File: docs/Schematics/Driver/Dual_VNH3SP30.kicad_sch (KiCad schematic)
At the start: 0 parts

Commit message: Add Wheel encoder
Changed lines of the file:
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@@
   (junction (at 76.2 53.34) (diameter 0) (color 0 0 0 0)
   )
-  (junction (at 132.08 62.23) (diameter 0) (color 0 0 0 0)
-  )
   (junction (at 80.01 50.8) (diameter 0) (color 0 0 0 0)
-  )
-  (junction (at 81.28 53.34) (diameter 0) (color 0 0 0 0)
   )
   (wire (pts (xy 115.57 55.88) (xy 132.08 55.88))
@@
     (stroke (width 0) (type default) (color 0 0 0 0))
   )
-  (wire (pts (xy 76.2 53.34) (xy 81.28 53.34))
-    (stroke (width 0) (type default) (color 0 0 0 0))
-  )
   (wire (pts (xy 115.57 80.01) (xy 132.08 80.01))
-    (stroke (width 0) (type default) (color 0 0 0 0))
-  )
-  (wire (pts (xy 132.08 62.23) (xy 81.28 62.23))
     (stroke (width 0) (type default) (color 0 0 0 0))
   )
@@
     (stroke (width 0) (type default) (color 0 0 0 0))
   )
-  (wire (pts (xy 81.28 53.34) (xy 83.82 53.34))
+  (wire (pts (xy 76.2 53.34) (xy 83.82 53.34))
     (stroke (width 0) (type default) (color 0 0 0 0))
   )
-  (wire (pts (xy 81.28 62.23) (xy 81.28 53.34))
-    (stroke (width 0) (type default) (color 0 0 0 0))
-  )

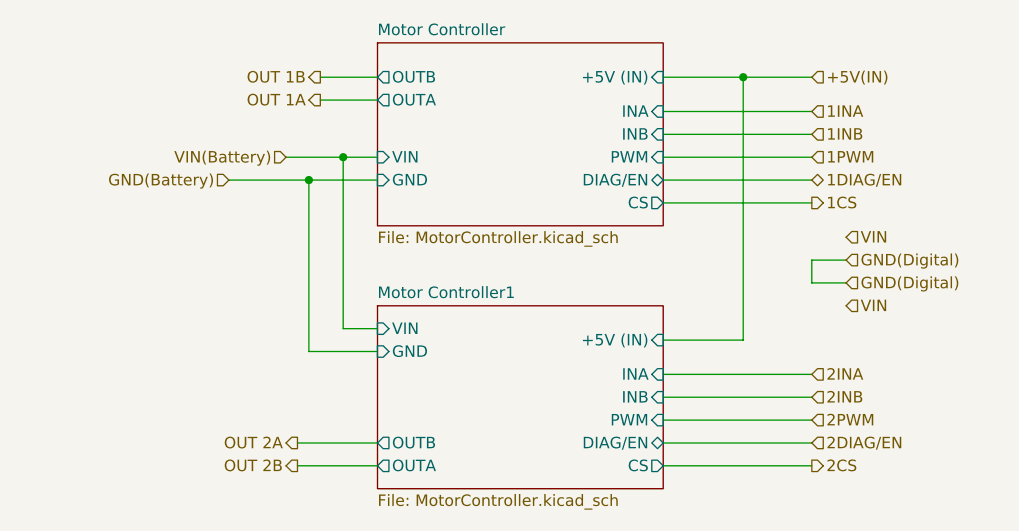
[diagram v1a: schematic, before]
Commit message: First scematic design for the card
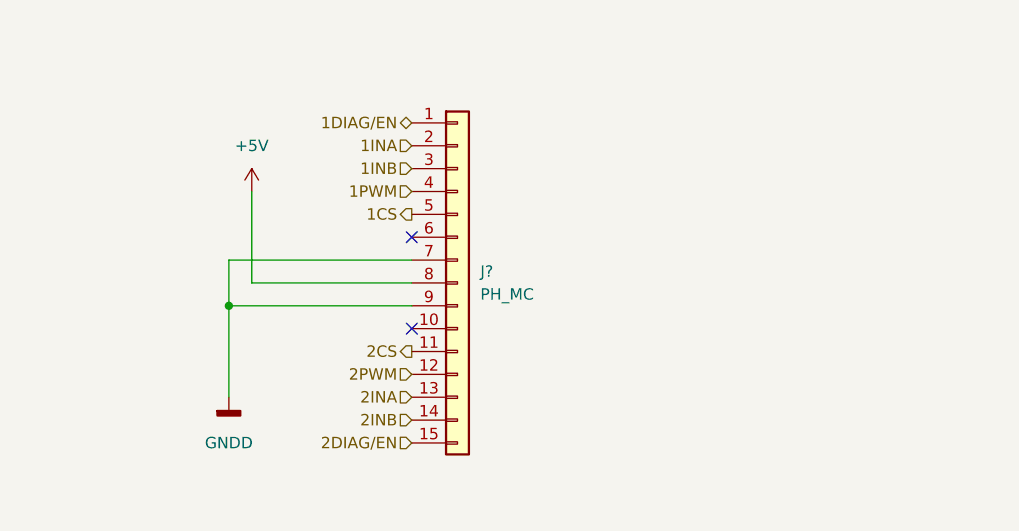
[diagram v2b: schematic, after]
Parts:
- added J?: PH_MC, symbol Connector_Generic:Conn_01x15
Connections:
- net 1CS: now also J?.5 (Pin_5)
- net 1DIAG/EN: now also J?.1 (Pin_1)
- net 1INA: now also J?.2 (Pin_2)
- net 1INB: now also J?.3 (Pin_3)
- net 1PWM: now also J?.4 (Pin_4)
- net 2CS: now also J?.11 (Pin_11)
- net 2DIAG/EN: now also J?.15 (Pin_15)
- net 2INA: now also J?.13 (Pin_13)
- net 2INB: now also J?.14 (Pin_14)
- net 2PWM: now also J?.12 (Pin_12)
- new net +5V: J?.8 (Pin_8)
- new net GNDD: J?.7 (Pin_7), J?.9 (Pin_9)
- no-connect marks 0 -> 2
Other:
- removed sheet Motor Controller
- removed sheet Motor Controller1
- company: (none) -> HiQ
- title: (none) -> Arty Z7 IO expander card

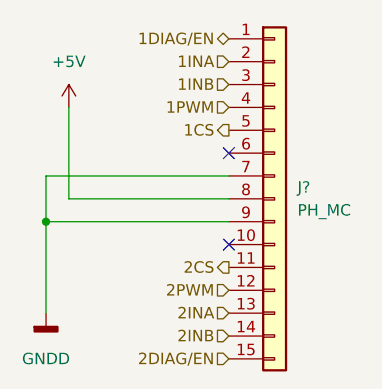
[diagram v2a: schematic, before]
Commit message: Added footprints and a symbol for the level shifters
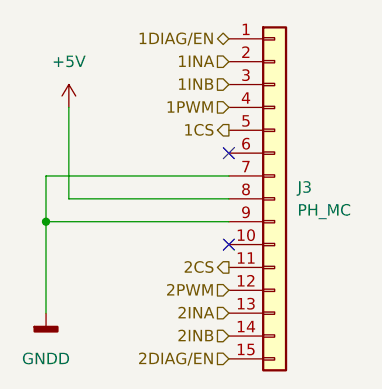
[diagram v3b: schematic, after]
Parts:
- J3: renamed from J?; footprint (none) -> Connector_PinHeader_2.54mm:PinHeader_1x15_P2.54mm_Vertical
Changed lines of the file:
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@@
   (symbol (lib_id "power:GNDD") (at 67.31 77.47 0) (unit 1)
     (in_bom yes) (on_board yes) (fields_autoplaced)
-    (property "Reference" "#PWR?" (id 0) (at 67.31 83.82 0)
+    (property "Reference" "#PWR05" (id 0) (at 67.31 83.82 0)
       (effects (font (size 1.27 1.27)) hide)
     )
@@
   (symbol (lib_id "Connector_Generic:Conn_01x15") (at 92.71 64.77 0) (unit 1)
     (in_bom yes) (on_board yes) (fields_autoplaced)
-    (property "Reference" "J?" (id 0) (at 95.25 63.4999 0)
+    (property "Reference" "J3" (id 0) (at 95.25 63.4999 0)
       (effects (font (size 1.27 1.27)) (justify left))
     )
@@
       (effects (font (size 1.27 1.27)) (justify left))
     )
-    (property "Footprint" "" (id 2) (at 92.71 64.77 0)
+    (property "Footprint" "Connector_PinHeader_2.54mm:PinHeader_1x15_P2.54mm_Vertical" (id 2) (at 92.71 64.77 0)
       (effects (font (size 1.27 1.27)) hide)
     )
@@
   (symbol (lib_id "power:+5V") (at 69.85 54.61 0) (unit 1)
     (in_bom yes) (on_board yes) (fields_autoplaced)
-    (property "Reference" "#PWR?" (id 0) (at 69.85 58.42 0)
+    (property "Reference" "#PWR06" (id 0) (at 69.85 58.42 0)
       (effects (font (size 1.27 1.27)) hide)
     )

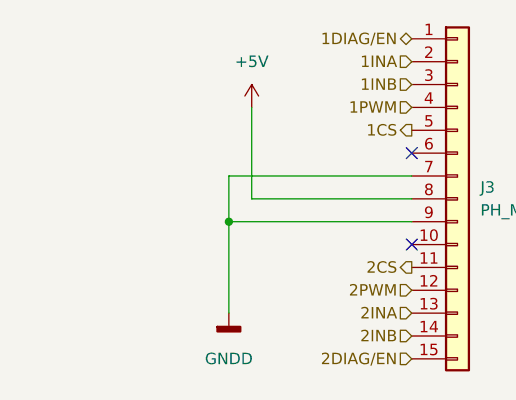
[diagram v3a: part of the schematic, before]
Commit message: Added caps and changed the connection from the motor sensors to plints
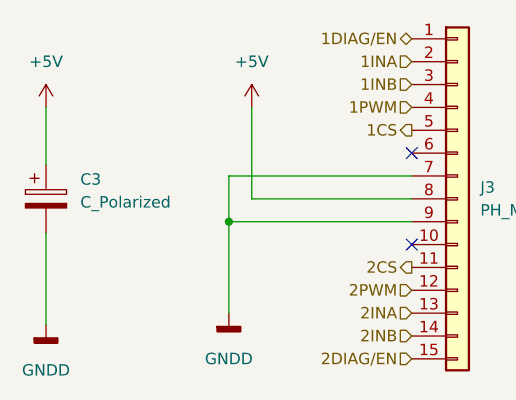
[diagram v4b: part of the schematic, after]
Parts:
- added C3: C_Polarized, Capacitor_THT:CP_Radial_D6.3mm_P2.50mm, symbol Device:C_Polarized
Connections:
- net +5V: now also C3.1
- net GNDD: now also C3.2
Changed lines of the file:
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@@
     (stroke (width 0) (type default) (color 0 0 0 0))
   )
+  (wire (pts (xy 46.99 68.58) (xy 46.99 78.74))
+    (stroke (width 0) (type default) (color 0 0 0 0))
+  )
   (wire (pts (xy 67.31 62.23) (xy 87.63 62.23))
     (stroke (width 0) (type default) (color 0 0 0 0))
@@
     (stroke (width 0) (type default) (color 0 0 0 0))
   )
+  (wire (pts (xy 46.99 54.61) (xy 46.99 60.96))
+    (stroke (width 0) (type default) (color 0 0 0 0))
+  )
   (wire (pts (xy 69.85 64.77) (xy 87.63 64.77))
     (stroke (width 0) (type default) (color 0 0 0 0))
@@
     (effects (font (size 1.27 1.27)) (justify right))
   )
+  (symbol (lib_id "Device:C_Polarized") (at 46.99 64.77 0) (unit 1)
+    (in_bom yes) (on_board yes) (fields_autoplaced)
+    (property "Reference" "C3" (id 0) (at 50.8 62.6109 0)
+      (effects (font (size 1.27 1.27)) (justify left))
+    )
+    (property "Value" "C_Polarized" (id 1) (at 50.8 65.1509 0)
+      (effects (font (size 1.27 1.27)) (justify left))
+    )
+    (property "Footprint" "Capacitor_THT:CP_Radial_D6.3mm_P2.50mm" (id 2) (at 47.9552 68.58 0)
+      (effects (font (size 1.27 1.27)) hide)
+    )
+    (property "Datasheet" "~" (id 3) (at 46.99 64.77 0)
+      (effects (font (size 1.27 1.27)) hide)
+    )
+    (pin "1")
+    (pin "2")
+  )
+  (symbol (lib_id "power:GNDD") (at 46.99 78.74 0) (unit 1)
+    (in_bom yes) (on_board yes) (fields_autoplaced)
+    (property "Reference" "#PWR044" (id 0) (at 46.99 85.09 0)
+      (effects (font (size 1.27 1.27)) hide)
+    )
+    (property "Value" "GNDD" (id 1) (at 46.99 83.82 0))
+    (property "Footprint" "" (id 2) (at 46.99 78.74 0)
+      (effects (font (size 1.27 1.27)) hide)
+    )
+    (property "Datasheet" "" (id 3) (at 46.99 78.74 0)
+      (effects (font (size 1.27 1.27)) hide)
+    )
+    (pin "1")
+  )
   (symbol (lib_id "power:GNDD") (at 67.31 77.47 0) (unit 1)
     (in_bom yes) (on_board yes) (fields_autoplaced)
@@
       (effects (font (size 1.27 1.27)) hide)
     )
+    (pin "1")
+  )
+  (symbol (lib_id "power:+5V") (at 46.99 54.61 0) (unit 1)
+    (in_bom yes) (on_board yes) (fields_autoplaced)
+    (property "Reference" "#PWR043" (id 0) (at 46.99 58.42 0)
+      (effects (font (size 1.27 1.27)) hide)
+    )
+    (property "Value" "+5V" (id 1) (at 46.99 49.53 0))
+    (property "Footprint" "" (id 2) (at 46.99 54.61 0)
+      (effects (font (size 1.27 1.27)) hide)
+    )
+    (property "Datasheet" "" (id 3) (at 46.99 54.61 0)
+      (effects (font (size 1.27 1.27)) hide)
+    )

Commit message: Started routing the pcb.
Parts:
- C3: footprint Capacitor_THT:CP_Radial_D6.3mm_P2.50mm -> Capacitor_SMD:C_0805_2012Metric_Pad1.18x1.45mm_HandSolder
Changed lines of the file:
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@@
       (effects (font (size 1.27 1.27)) (justify left))
     )
-    (property "Footprint" "Capacitor_THT:CP_Radial_D6.3mm_P2.50mm" (id 2) (at 47.9552 68.58 0)
+    (property "Footprint" "Capacitor_SMD:C_0805_2012Metric_Pad1.18x1.45mm_HandSolder" (id 2) (at 47.9552 68.58 0)
       (effects (font (size 1.27 1.27)) hide)
     )

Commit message: First version of the routed board is done
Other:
- title: Arty Z7 IO expander card -> Arty Z7 IO Board
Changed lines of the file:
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@@
   (paper "A4")
   (title_block
-    (title "Arty Z7 IO expander card")
+    (title "Arty Z7 IO Board")
     (date "2022-12-24")
-    (rev "0.1")
+    (rev "${VER}")
     (company "HiQ")
   )
